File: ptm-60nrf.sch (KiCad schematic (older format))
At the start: 24 parts, among them J1 USB_C_Receptacle_USB2.0, J2 BAT, J3 Conn_01x04_Male, J4 SWD, Q1 AO3407, U1 TP4054, U2 XC6220B331MR-G, U3 nRF52840_holyiot_18010, U4 SRV05-4

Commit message: updated README
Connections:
- net COL10: now also U3.28 (P1.03); no longer U3.30 (P1.02)
- net COL11: now also U3.29 (P1.01); no longer U3.33 (P1.04)
- net COL12: now also U3.30 (P1.02); no longer U3.34 (P1.06)
- net COL13: now also U3.33 (P1.04); no longer U3.35 (P0.09)
- net COL14: now also U3.34 (P1.06); no longer U3.36 (P0.10)
- net COL9: now also U3.27 (P1.00); no longer U3.29 (P1.01)
- net ROW4: now also U3.26 (P0.22); no longer U3.28 (P1.03)
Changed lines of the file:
@@
 Text GLabel 2800 6650 3    50   Input ~ 0
 ROW3
-Text GLabel 3800 5700 2    50   Input ~ 0
+Text GLabel 3800 5900 2    50   Input ~ 0
 ROW4
-Wire Wire Line
-	3800 4900 3700 4900
-Wire Wire Line
-	3800 5000 3700 5000
 Wire Wire Line
 	3800 5100 3700 5100
@@
 Text GLabel 2700 6650 3    50   Output ~ 0
 COL8
-Wire Wire Line
-	3800 5700 3700 5700
+Text GLabel 3800 5800 2    50   Output ~ 0
+COL9
+Wire Wire Line
+	2200 5400 2300 5400
+Text GLabel 3800 5100 2    50   Output ~ 0
+COL14
+Wire Wire Line
+	2200 5900 2300 5900
+Text GLabel 3800 5200 2    50   Output ~ 0
+COL13
+Wire Wire Line
+	2200 5800 2300 5800
+Text GLabel 3800 5500 2    50   Output ~ 0
+COL12
+Wire Wire Line
+	2200 5700 2300 5700
 Text GLabel 3800 5600 2    50   Output ~ 0
-COL9
-Wire Wire Line
-	2200 5400 2300 5400
-Text GLabel 3800 4900 2    50   Output ~ 0
-COL14
-Wire Wire Line
-	2200 5900 2300 5900
-Text GLabel 3800 5000 2    50   Output ~ 0
-COL13
-Wire Wire Line
-	2200 5800 2300 5800
-Text GLabel 3800 5100 2    50   Output ~ 0
-COL12
-Wire Wire Line
-	2200 5700 2300 5700
-Text GLabel 3800 5200 2    50   Output ~ 0
 COL11
 Wire Wire Line
 	2200 5600 2300 5600
-Text GLabel 3800 5500 2    50   Output ~ 0
+Text GLabel 3800 5700 2    50   Output ~ 0
 COL10
 Wire Wire Line
@@
 NoConn ~ 3700 4500
 NoConn ~ 3700 4600
-NoConn ~ 3700 5800
-NoConn ~ 3700 5900
 NoConn ~ 4500 1900
 NoConn ~ 4300 1900
@@
 Text GLabel 6900 1600 2    50   Input ~ 0
 VB
+Wire Wire Line
+	3800 5700 3700 5700
+Wire Wire Line
+	3800 5800 3700 5800
+Wire Wire Line
+	3800 5900 3700 5900
+NoConn ~ 3700 5000
+NoConn ~ 3700 4900
 $EndSCHEMATC

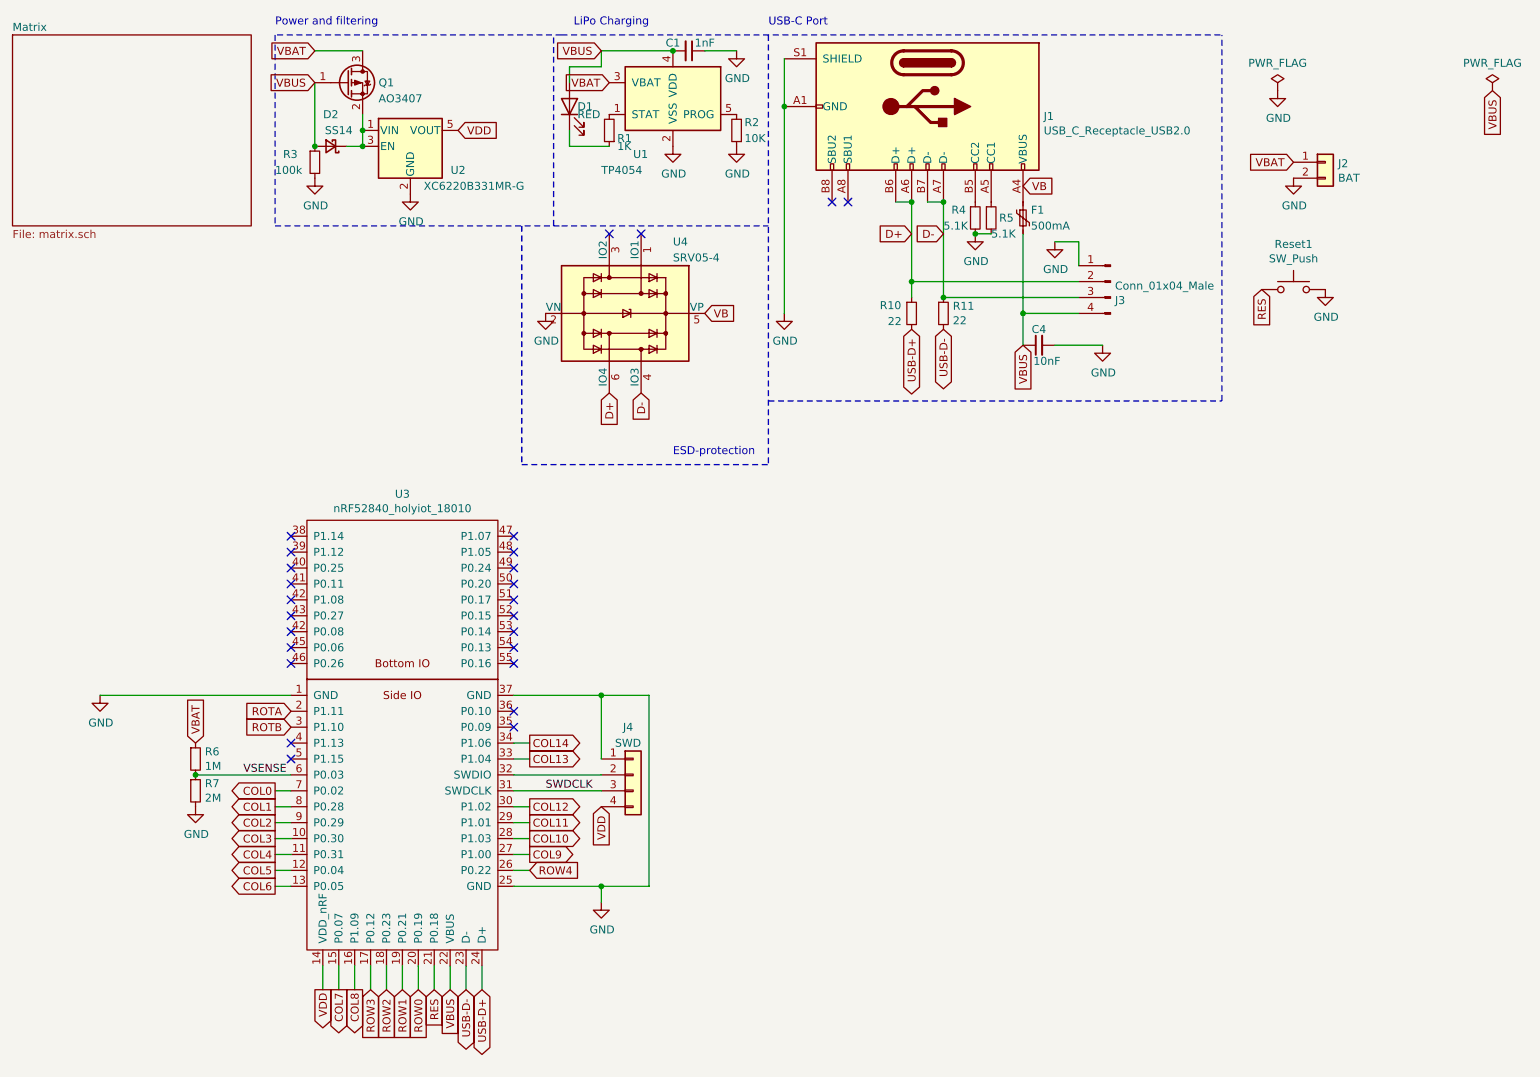
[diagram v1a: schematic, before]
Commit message: swapped polarity on battery connector… Other minor fixes
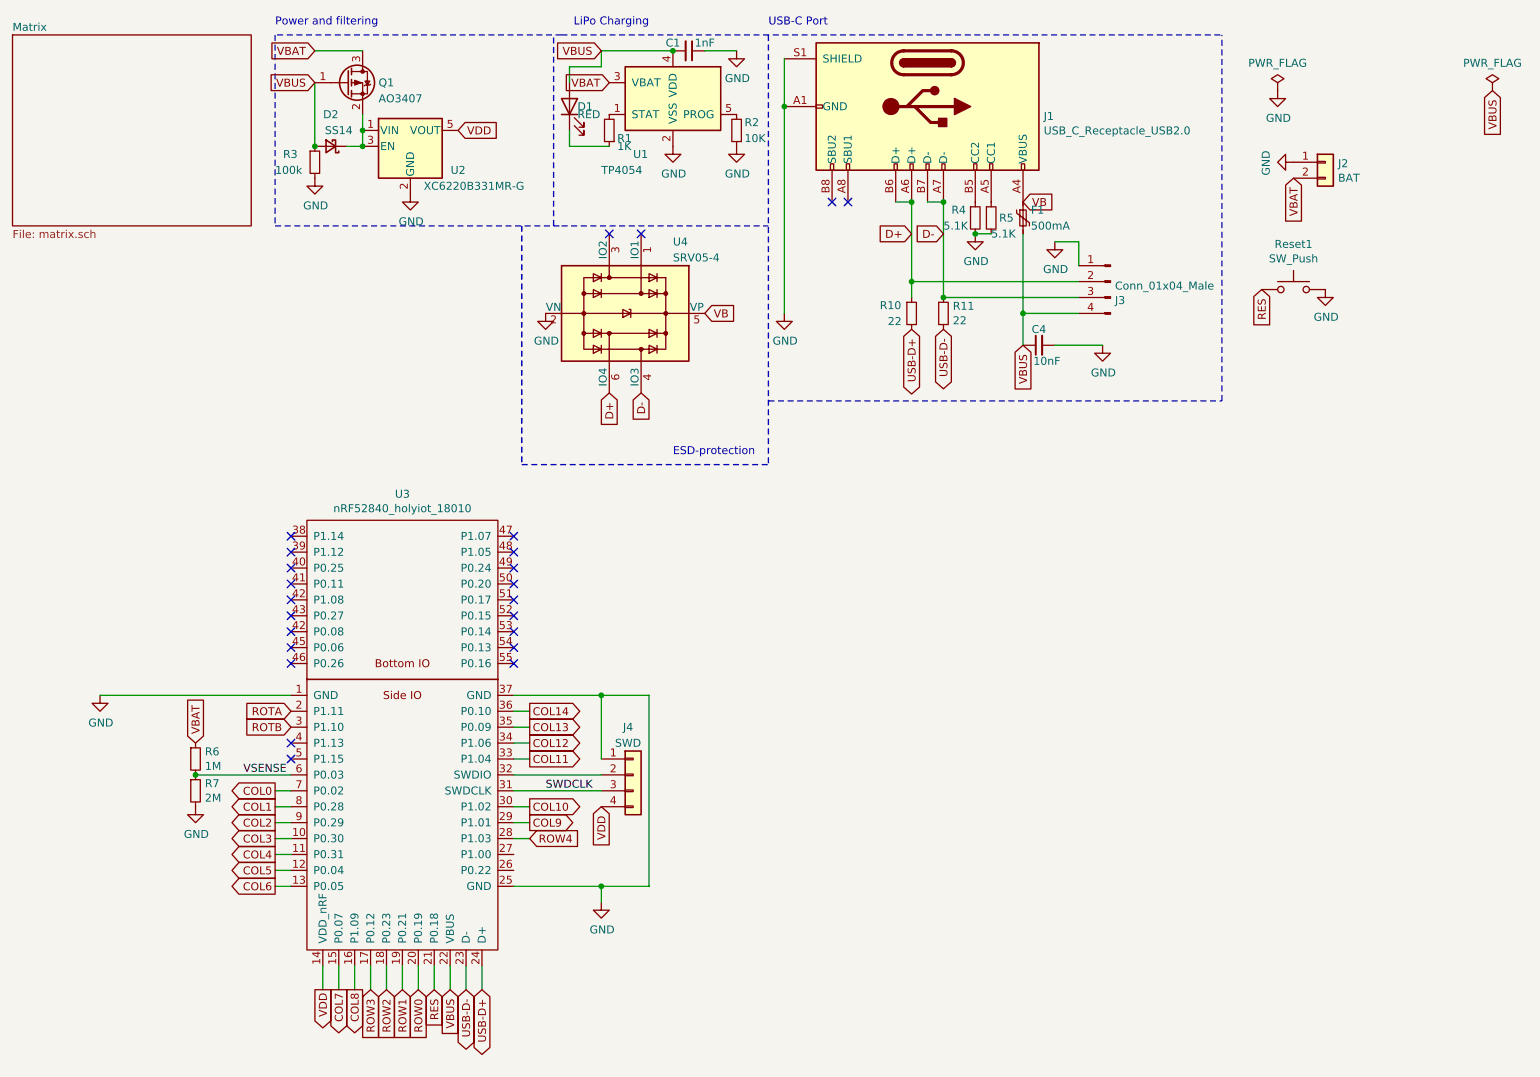
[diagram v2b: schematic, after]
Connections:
- net COL10: now also U3.30 (P1.02); no longer U3.28 (P1.03)
- net COL11: now also U3.33 (P1.04); no longer U3.29 (P1.01)
- net COL12: now also U3.34 (P1.06); no longer U3.30 (P1.02)
- net COL13: now also U3.35 (P0.09); no longer U3.33 (P1.04)
- net COL14: now also U3.36 (P0.10); no longer U3.34 (P1.06)
- net COL9: now also U3.29 (P1.01); no longer U3.27 (P1.00)
- net GND: now also J2.1 (Pin_1); no longer J2.2 (Pin_2)
- net ROW4: now also U3.28 (P1.03); no longer U3.26 (P0.22)
- net VB: now also F1.1, J1.A4 (VBUS), J1.A9 (VBUS), J1.B4 (VBUS), J1.B9 (VBUS)
- net VBAT: now also J2.2 (Pin_2); no longer J2.1 (Pin_1)
- no-connect marks 26 -> 24
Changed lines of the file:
@@
 Text GLabel 2800 6650 3    50   Input ~ 0
 ROW3
-Text GLabel 3800 5900 2    50   Input ~ 0
+Text GLabel 3800 5700 2    50   Input ~ 0
 ROW4
 Wire Wire Line
+	3800 4900 3700 4900
+Wire Wire Line
+	3800 5000 3700 5000
+Wire Wire Line
 	3800 5100 3700 5100
-Wire Wire Line
-	3800 5200 3700 5200
-Wire Wire Line
-	3800 5500 3700 5500
 Text GLabel 2200 6000 0    50   Output ~ 0
 COL6
@@
 Text GLabel 2700 6650 3    50   Output ~ 0
 COL8
-Text GLabel 3800 5800 2    50   Output ~ 0
+Text GLabel 3800 5600 2    50   Output ~ 0
 COL9
 Wire Wire Line
 	2200 5400 2300 5400
+Text GLabel 3800 4900 2    50   Output ~ 0
+COL14
+Wire Wire Line
+	2200 5900 2300 5900
+Text GLabel 3800 5000 2    50   Output ~ 0
+COL13
+Wire Wire Line
+	2200 5800 2300 5800
 Text GLabel 3800 5100 2    50   Output ~ 0
-COL14
-Wire Wire Line
-	2200 5900 2300 5900
+COL12
+Wire Wire Line
+	2200 5700 2300 5700
 Text GLabel 3800 5200 2    50   Output ~ 0
-COL13
-Wire Wire Line
-	2200 5800 2300 5800
+COL11
+Wire Wire Line
+	2200 5600 2300 5600
 Text GLabel 3800 5500 2    50   Output ~ 0
-COL12
-Wire Wire Line
-	2200 5700 2300 5700
-Text GLabel 3800 5600 2    50   Output ~ 0
-COL11
-Wire Wire Line
-	2200 5600 2300 5600
-Text GLabel 3800 5700 2    50   Output ~ 0
 COL10
 Wire Wire Line
@@
 L power:GND #PWR06
 U 1 1 610B8E3D
-P 8600 1550
-F 0 "#PWR06" H 8600 1300 50  0001 C CNN
-F 1 "GND" H 8605 1377 50  0000 C CNN
-F 2 "" H 8600 1550 50  0001 C CNN
-F 3 "" H 8600 1550 50  0001 C CNN
-	1    8600 1550
-	1    0    0    -1
-$EndComp
-Text GLabel 8600 1450 0    50   Input ~ 0
+P 8600 1450
+F 0 "#PWR06" H 8600 1200 50  0001 C CNN
+F 1 "GND" H 8605 1277 50  0000 C CNN
+F 2 "" H 8600 1450 50  0001 C CNN
+F 3 "" H 8600 1450 50  0001 C CNN
+	1    8600 1450
+	0    1    1    0
+$EndComp
+Text GLabel 8600 1550 3    50   Input ~ 0
 VBAT
 Wire Wire Line
@@
 	6400 1700 6400 2300
 Wire Wire Line
-	3800 5600 3700 5600
+	3800 5200 3700 5200
 Wire Wire Line
 	4250 5200 4250 4800
@@
 Text GLabel 6400 1900 0    50   Input ~ 0
 D-
-Text GLabel 6900 1600 2    50   Input ~ 0
+Text GLabel 6900 1700 2    50   Input ~ 0
 VB
 Wire Wire Line
+	3800 5500 3700 5500
+Wire Wire Line
+	3800 5600 3700 5600
+Wire Wire Line
 	3800 5700 3700 5700
-Wire Wire Line
-	3800 5800 3700 5800
-Wire Wire Line
-	3800 5900 3700 5900
-NoConn ~ 3700 5000
-NoConn ~ 3700 4900
 $EndSCHEMATC
